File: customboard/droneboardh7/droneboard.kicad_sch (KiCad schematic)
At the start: 56 parts, among them J1 Conn_01x04, J2 Conn_01x04, J3 Conn_01x05_Pin, J4 Conn_01x02_Pin, J5 USB_C_Receptacle_USB2.0_16P, J6 Conn_01x04, SW1 SW_Push, SW2 SW_Push, U2 STM32H723VGTx, U3 L78M05CDT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

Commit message: board work
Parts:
- added J7, J8, J9: Conn_01x01_Pin, TestPoint:TestPoint_Pad_2.5x2.5mm, symbol Connector:Conn_01x01_Pin
- J4: footprint Connector_PinHeader_1.27mm:PinHeader_1x02_P1.27mm_Vertical -> Connector_PinHeader_2.54mm:PinHeader_1x02_P2.54mm_Vertical
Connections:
- net GND: now also J9.1 (Pin_1)
- net SWDIO: now reaches U2.72 (PA13(JTMS)
- net SWDIO: now also J8.1 (Pin_1)
- net SWCLK: now reaches U2.76 (PA14(JTCK)
- net SWCLK: now also J7.1 (Pin_1)
- no-connect marks 64 -> 62

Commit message: h7 hardware done
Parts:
- R7, R8: footprint Resistor_SMD:R_0402_1005Metric -> Resistor_SMD:R_0603_1608Metric
- U3: value L78M05CDT -> LM7805MPX; footprint Package_TO_SOT_SMD:TO-252-2 -> Package_TO_SOT_SMD:SOT-223-3_TabPin2
- U5, U6: value LDK130M33R -> SPX3819M5-L-3-3; symbol Regulator_Linear:LDK130-33_SOT23_SOT353 -> Regulator_Linear:SPX3819M5-L-3-3
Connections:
- net BLUE: now also U2.2 (PE3); no longer U2.15 (PC0)
- net GND: now also U3.3 (OUT)
- net GREEN: now also U2.1 (PE2); no longer U2.7 (PC13)
- net IMU_CS: now also U2.93 (PB7); no longer U2.8 (PC14)
- net MISO: now also U2.90 (PB4(NJTRST)); no longer U2.4 (PE5)
- net MOSI: now also U2.91 (PB5); no longer U2.5 (PE6)
- net SCK: now also U2.89 (PB3(JTDO); no longer U2.1 (PE2)
- net VMCU: now also U2.20 (VREF+)
- net YELLOW: now also U2.3 (PE4); no longer U2.16 (PC1)
- net at R11.1: now also J5.B5 (CC2); no longer J5.B8 (SBU2)
- net at R10.1: now also J5.A5 (CC1); no longer J5.A8 (SBU1)
- no-connect marks 62 -> 61
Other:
- moved on the sheet: J3, R10, R11, SW1, SW2

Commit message: smps initial
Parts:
- removed C19: 330n, Capacitor_SMD:C_0805_2012Metric, symbol Device:C
- removed C20: 100n, Capacitor_SMD:C_0603_1608Metric, symbol Device:C
- removed U3: LM7805MPX, Package_TO_SOT_SMD:SOT-223-3_TabPin2, symbol Regulator_Linear:L7805
- added C13: 10u, Capacitor_SMD:C_1206_3216Metric, symbol Device:C
- added C14: 100n, Capacitor_SMD:C_0603_1608Metric, symbol Device:C
- added C17, C18: 22u, Capacitor_SMD:C_0805_2012Metric, symbol Device:C
- added L1: IFSC2020DZER4R7N01, Inductor_SMD:L_Vishay_IHLP-2020, symbol Device:L
- added U1: AP63205WU, Package_TO_SOT_SMD:TSOT-23-6, symbol Regulator_Switching:AP63205WU
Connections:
- net 12V: now also C13.1, U1.2 (EN), U1.3 (IN)
- net 5V: now also C17.1, C18.1, L1.2, U1.1 (FB)
- net GND: now also C13.2, C17.2, C18.2, U1.4 (GND)
- new net: C14.1, U1.6 (BST)
- new net: C14.2, L1.1, U1.5 (SW)

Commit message: smps complete
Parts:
- removed J7, J8, J9: Conn_01x01_Pin, TestPoint:TestPoint_Pad_2.5x2.5mm, symbol Connector:Conn_01x01_Pin
- added J10: Conn_01x03_Pin, Connector_PinHeader_2.54mm:PinHeader_1x03_P2.54mm_Vertical, symbol Connector:Conn_01x03_Pin
- L1: value IFSC2020DZER4R7N01 -> IHLP2020CZER4R7M11
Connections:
- net GND: now also J10.1 (Pin_1)
- net SWCLK: now also J10.3 (Pin_3)
- net SWDIO: now also J10.2 (Pin_2)

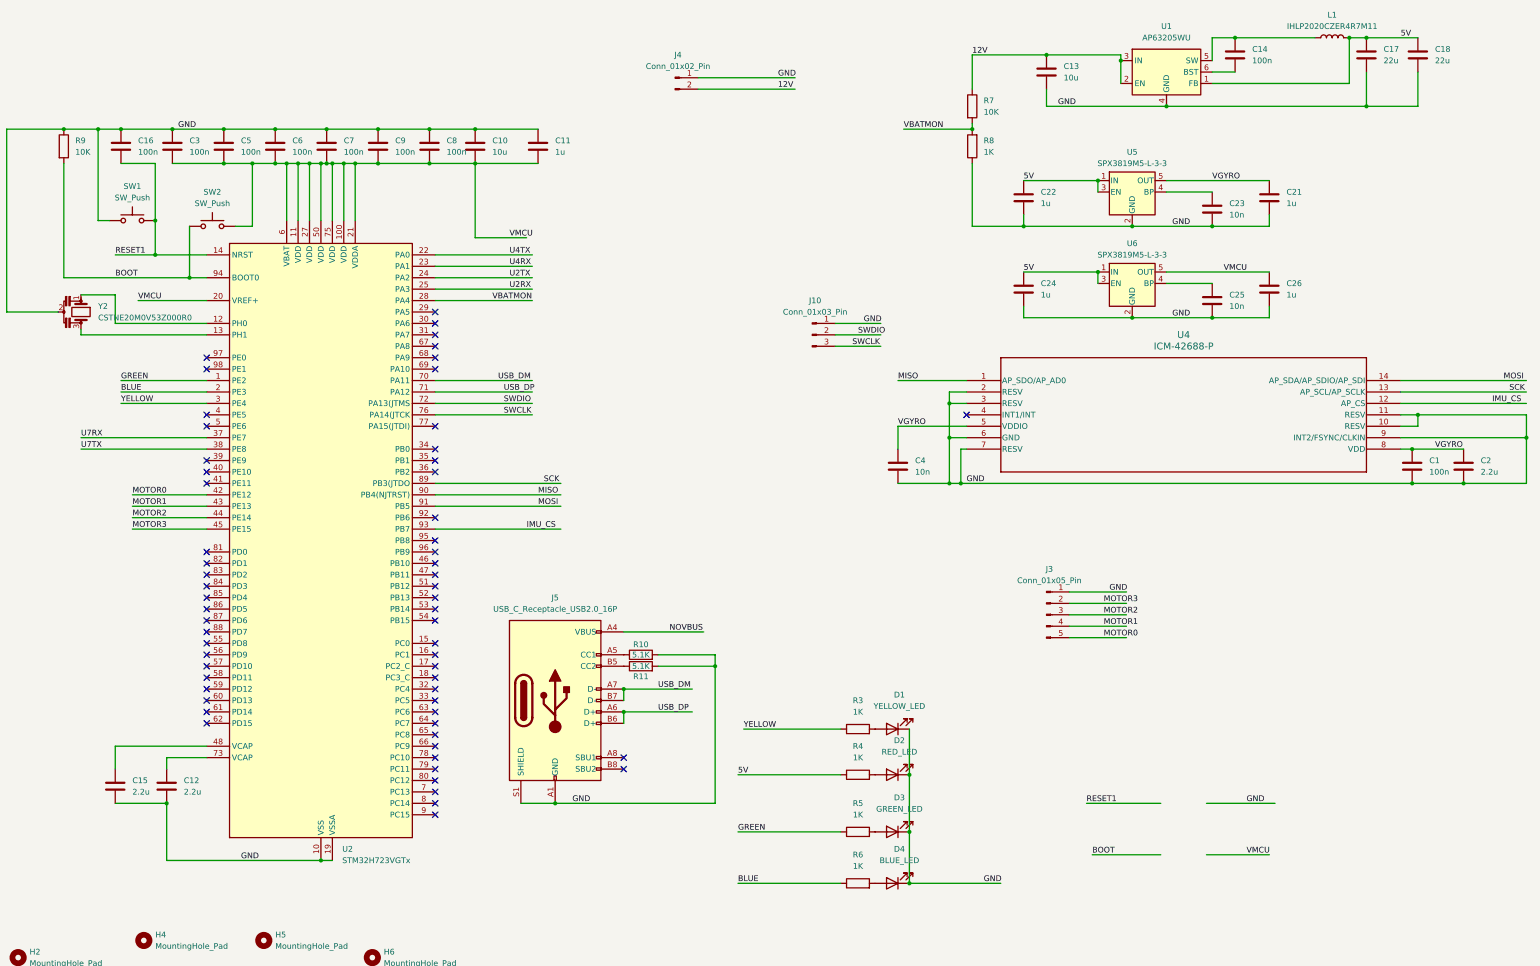
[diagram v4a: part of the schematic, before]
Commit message: SMA TOP; 20mm VTX; 3A SMPS; MSP OSD
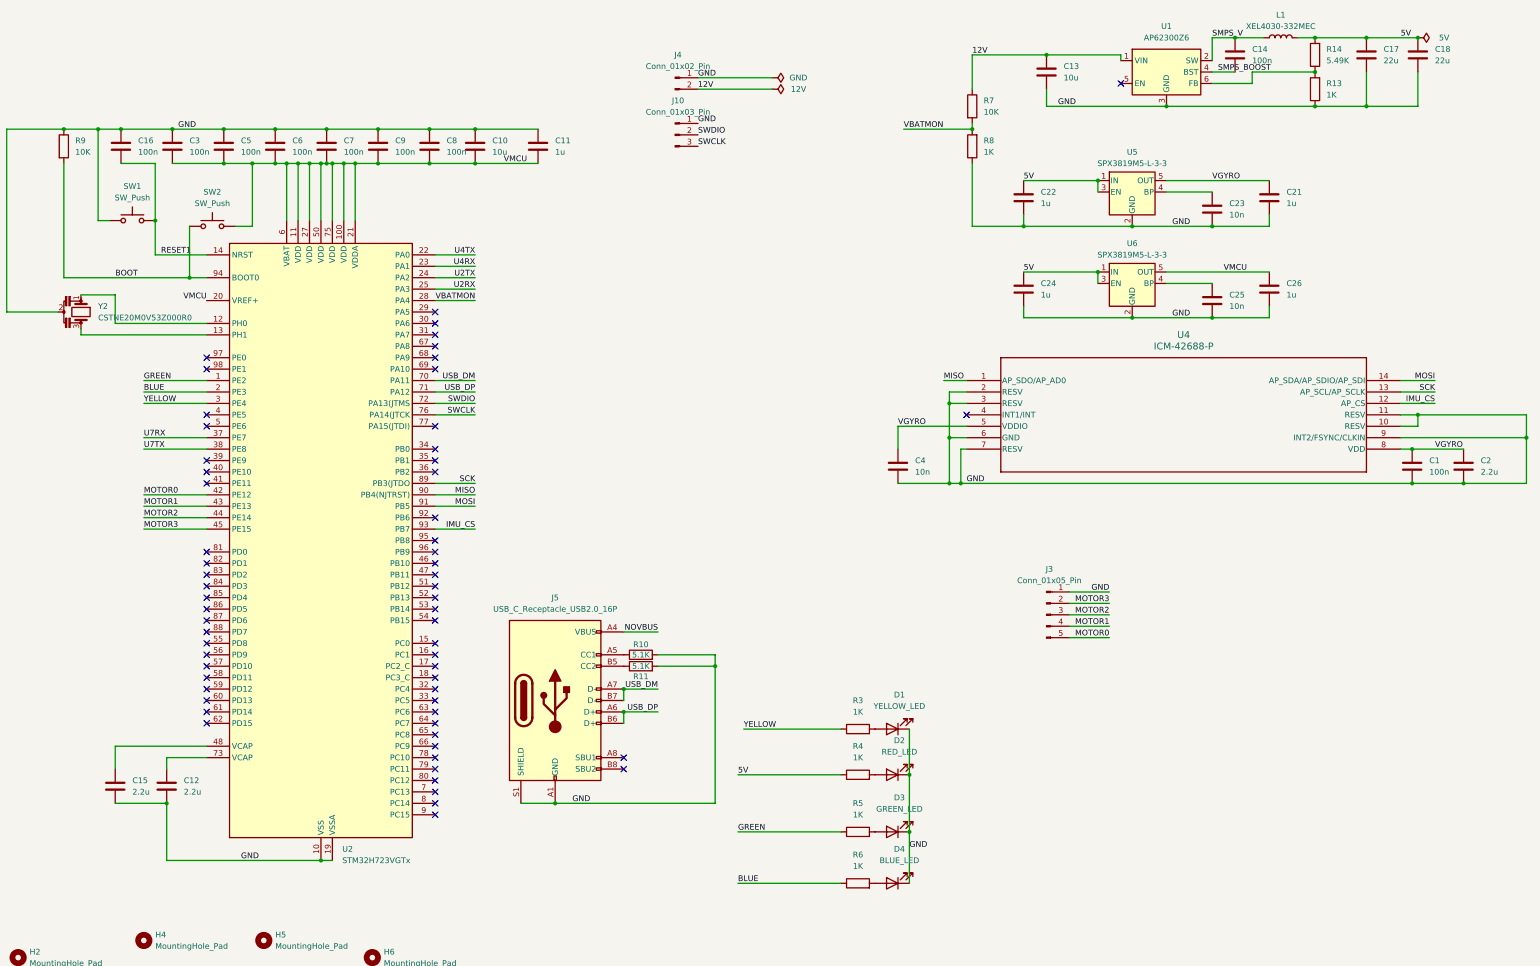
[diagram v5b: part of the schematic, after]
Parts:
- removed U1: AP63205WU, Package_TO_SOT_SMD:TSOT-23-6, symbol Regulator_Switching:AP63205WU
- added R13: 1K, Resistor_SMD:R_0402_1005Metric, symbol Device:R
- added R14: 5.49K, Resistor_SMD:R_0402_1005Metric, symbol Device:R
- added U1: AP62300Z6, Package_TO_SOT_SMD:SOT-563, symbol Regulator_Switching:AP62300Z6
- C13: footprint Capacitor_SMD:C_1206_3216Metric -> Capacitor_SMD:C_0603_1608Metric
- C17, C18: footprint Capacitor_SMD:C_0805_2012Metric -> Capacitor_SMD:C_0603_1608Metric
- L1: value IHLP2020CZER4R7M11 -> XEL4030-332MEC; footprint Inductor_SMD:L_Vishay_IHLP-2020 -> Inductor_SMD:L_Coilcraft_XxL4030
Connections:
- net 12V: now also U1.1 (VIN)
- net 5V: now also R14.2
- net GND: now also R13.1, U1.3 (GND)
- net SMPS_BOOST: now reaches C14.1
- net SMPS_BOOST: now also U1.4 (BST)
- net SMPS_V: now reaches C14.2, L1.1
- net SMPS_V: now also U1.2 (SW)
- new net: R13.2, R14.1, U1.6 (FB)
- no-connect marks 61 -> 62
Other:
- moved on the sheet: J10, L1
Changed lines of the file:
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@@
 (kicad_sch
-	(version 20231120)
+	(version 20250114)
 	(generator "eeschema")
-	(generator_version "8.0")
+	(generator_version "9.0")
 	(paper "A1")

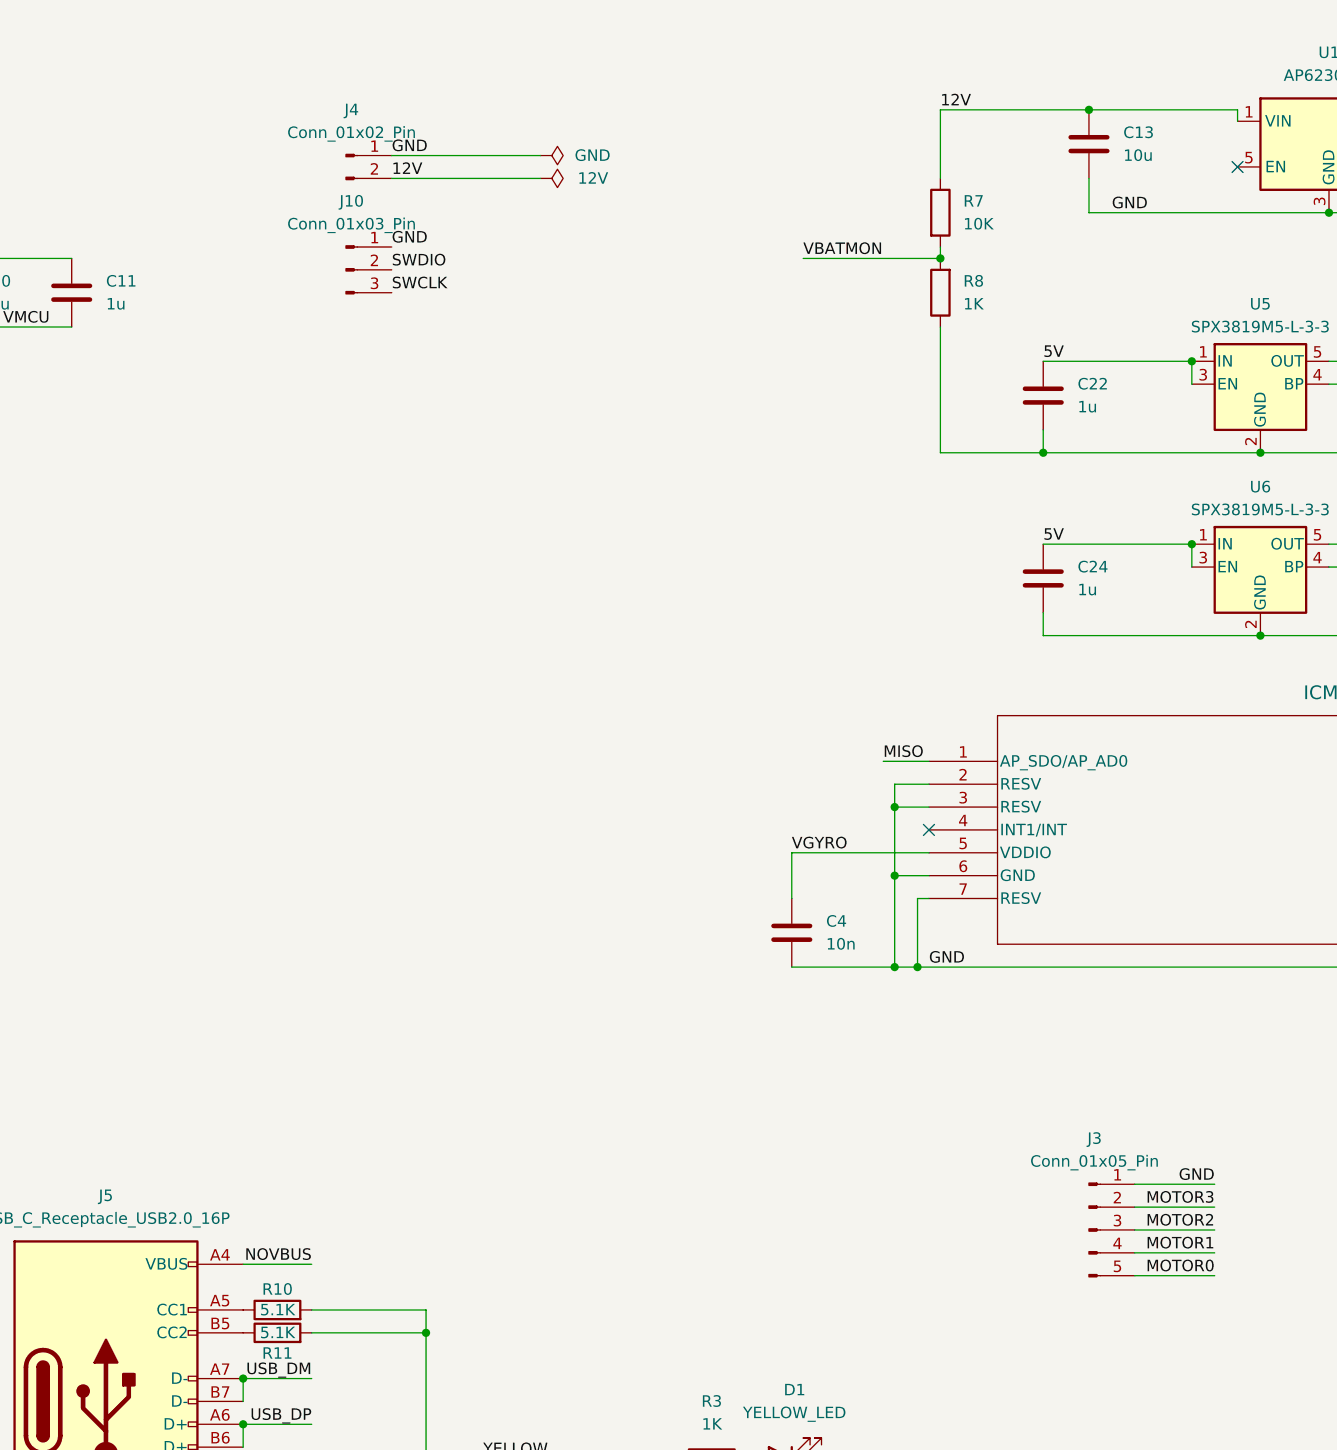
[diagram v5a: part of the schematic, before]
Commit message: battery/telemetry separation, parallel dshot, wider pin headers
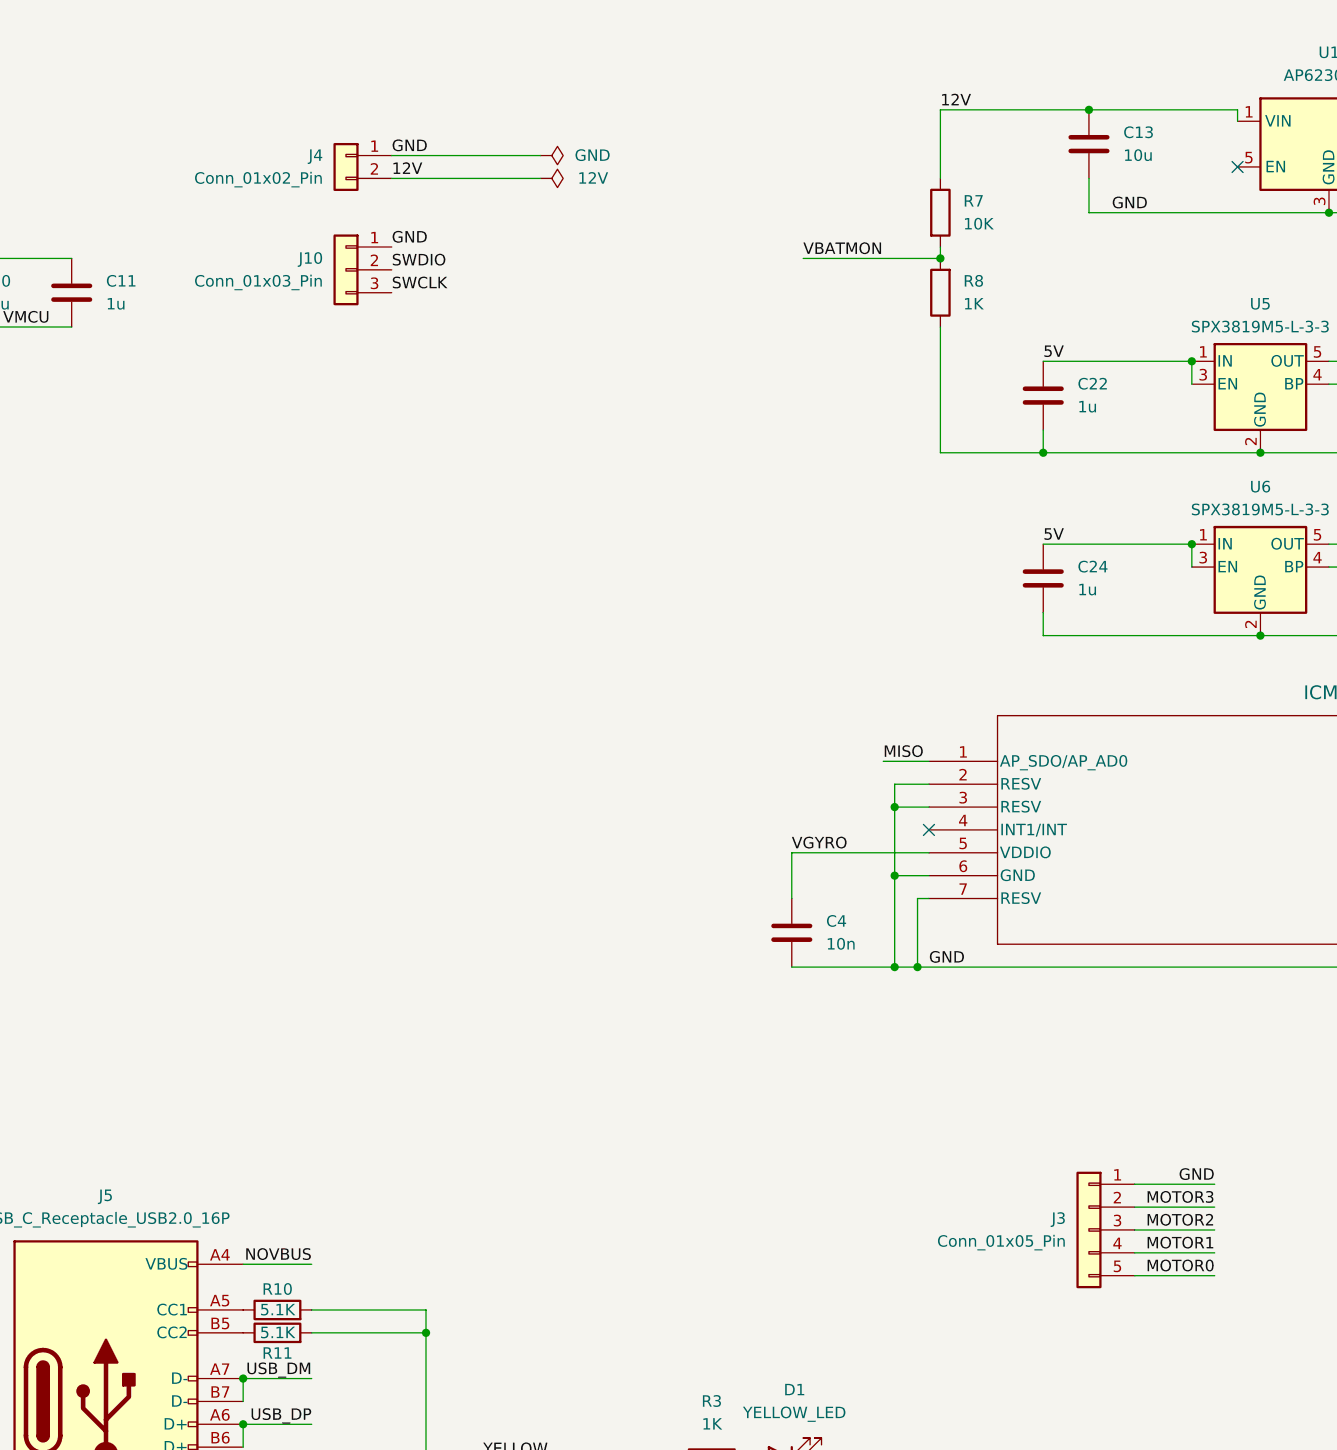
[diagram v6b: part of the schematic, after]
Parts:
- J1, J2, J6: footprint Connector_PinHeader_1.27mm:PinHeader_1x04_P1.27mm_Vertical -> Custom:PinHeaderWide4x
- J10: symbol Connector:Conn_01x03_Pin -> Connector_Generic:Conn_01x03
- J3: footprint Connector_PinHeader_1.27mm:PinHeader_1x05_P1.27mm_Vertical -> Custom:PinHeaderWide5x; symbol Connector:Conn_01x05_Pin -> Connector_Generic:Conn_01x05
- J4: symbol Connector:Conn_01x02_Pin -> Connector_Generic:Conn_01x02

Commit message: h723 further work
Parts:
- C13: value 10u -> 10u25VX7R; footprint Capacitor_SMD:C_0603_1608Metric -> Capacitor_SMD:C_1210_3225Metric
- C14: value 100n -> 100n25VX7R
- C17, C18: value 22u -> 22u10VX5R; footprint Capacitor_SMD:C_0603_1608Metric -> Capacitor_SMD:C_0805_2012Metric
- J3: footprint Custom:PinHeaderWide5x -> Connector_PinHeader_2.00mm:PinHeader_1x05_P2.00mm_Vertical
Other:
- moved on the sheet: C14, C17, C18, L1, R13, R14

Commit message: stuff
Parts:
- removed U2: STM32H723VGTx, Package_QFP:LQFP-100_14x14mm_P0.5mm, symbol MCU_ST_STM32H7:STM32H723VGTx
- added U3: STM32H743VITx, Package_QFP:LQFP-100_14x14mm_P0.5mm, symbol MCU_ST_STM32H7:STM32H743VITx
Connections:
- net BLUE: now also U3.2 (PE3)
- net BOOT: now also U3.94 (BOOT0)
- net GND: now also U3.10 (VSS), U3.19 (VSSA), U3.26 (VSS), U3.49 (VSS), U3.74 (VSS), U3.99 (VSS)
- net GREEN: now also U3.1 (PE2)
- net IMU_CS: now also U3.93 (PB7)
- net MISO: now also U3.90 (PB4)
- net MOSI: now also U3.91 (PB5)
- net MOTOR0: now also U3.42 (PE12)
- net MOTOR1: now also U3.43 (PE13)
- net MOTOR2: now also U3.44 (PE14)
- net MOTOR3: now also U3.45 (PE15)
- net RESET1: now also U3.14 (NRST)
- net SCK: now also U3.89 (PB3)
- net SWCLK: now also U3.76 (PA14)
- net SWDIO: now also U3.72 (PA13)
- net U2RX: now also U3.25 (PA3)
- net U2TX: now also U3.24 (PA2)
- net U4RX: now also U3.23 (PA1)
- net U4TX: now also U3.22 (PA0)
- net U7RX: now also U3.37 (PE7)
- net U7TX: now also U3.38 (PE8)
- net USB_DM: now also U3.70 (PA11)
- net USB_DP: now also U3.71 (PA12)
- net VBATMON: now also U3.28 (PA4)
- net VMCU: now also U3.100 (VDD), U3.11 (VDD), U3.20 (VREF+), U3.21 (VDDA), U3.27 (VDD), U3.50 (VDD), U3.6 (VBAT), U3.75 (VDD)
- net YELLOW: now also U3.3 (PE4)
- net at Y2.1: now also U3.12 (PH0)
- net at Y2.3: now also U3.13 (PH1)
- net at C12.1: now also U3.73 (VCAP)
- net at C15.1: now also U3.48 (VCAP)
